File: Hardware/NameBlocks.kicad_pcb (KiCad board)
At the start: 2 copper layers, 38.1 x 38.1 mm, 19 parts, among them J1 CONN_01X06, J2 CONN_01X05, J3 CONN_01X05, Q1 Q_NMOS_GSD, U1 ACPSA04-41SRWA-17406, U2 ATTiny828, U3 MAX16054

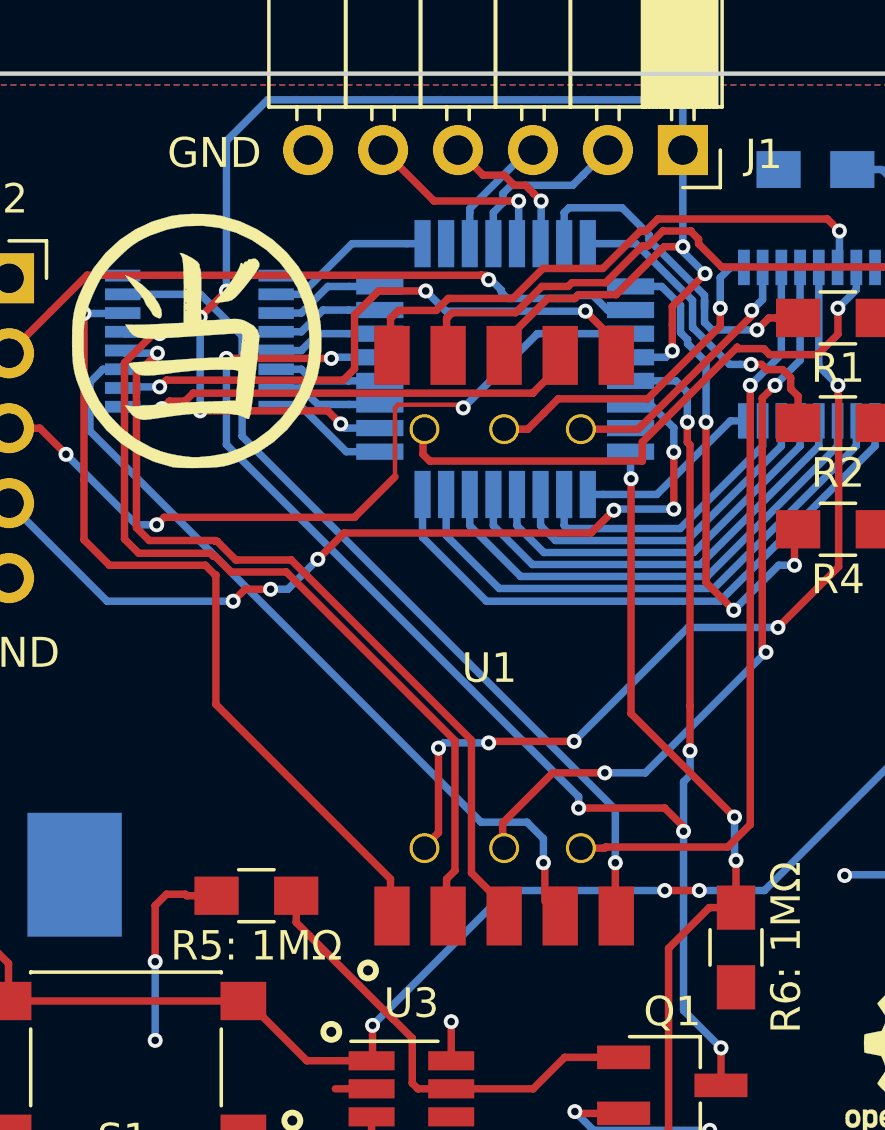
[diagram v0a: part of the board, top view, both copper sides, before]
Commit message: Shrank trace on Net-(RN2-Pad1) for pin 13 of display
Pins 13, 14, 15, 16 on the LED segment shorted together on two boards AFTER soldering the display down. I believe that is because trace Net-(RN2-Pad1) from pin 13 on the alphanumeric display was too close to pins 14, 15, 16, resulting in a short after soldering and when the display is pressed down. I changed that trace to 6 mils (from 10 mils) and moved it away from the problem zone.
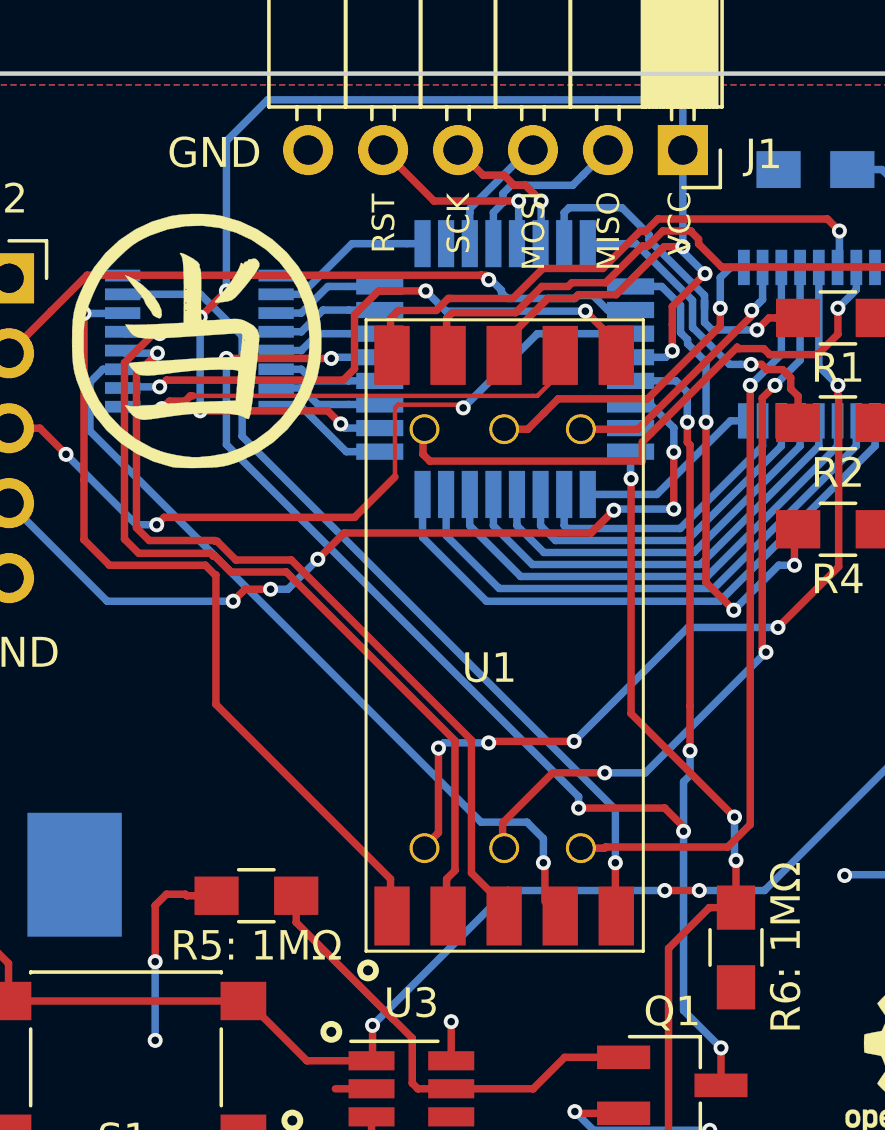
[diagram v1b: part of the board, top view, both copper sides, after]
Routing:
- net Net-(RN2-Pad1): track 15.8 -> 16.4 mm
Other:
- board text added: "1.1"
- board text added: "MISO"
- board text added: "MOSI"
- board text added: "March 2018, v1.1"
- board text added: "RST"
- board text added: "SCK"
- board text removed: "1.0"
- board text removed: "Feb 2018, v1.0"
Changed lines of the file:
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@@
     (area 68.821399 34.175799 271.609914 194.5424)
     (thickness 1.6)
-    (drawings 26)
-    (tracks 540)
+    (drawings 31)
+    (tracks 542)
     (zones 0)
     (modules 19)
@@
   (page A4)
   (layers
-    (0 F.Cu signal hide)
-    (31 B.Cu signal hide)
+    (0 F.Cu signal)
+    (31 B.Cu signal)
     (32 B.Adhes user)
     (33 F.Adhes user)
@@
     (47 F.CrtYd user)
     (48 B.Fab user hide)
-    (49 F.Fab user hide)
+    (49 F.Fab user)
   )
   (setup
@@
     (add_net "Net-(RN2-Pad7)")
     (add_net VCC)
+  )
+  (module ACPSA04_Alphanumeric_LED:ACPSA04_Alphanumeric_LED locked (layer F.Cu)
+    (at 91.7788 51.6124)
+    (fp_text reference U1 (at 3.8 10.6) (layer F.SilkS)
+      (effects (font (size 1 1) (thickness 0.15)))
+    )
+    (fp_text value ACPSA04-41SRWA-17406 (at 5.3 8.8) (layer F.Fab)
+      (effects (font (size 1 1) (thickness 0.15)))
+    )
+    (fp_line (start -0.381 20.193) (end -0.381 -1.2065) (layer F.SilkS) (width 0.1016))
+    (fp_line (start 9.017 20.193) (end -0.381 20.193) (layer F.SilkS) (width 0.1016))
+    (fp_line (start 9.017 -1.2065) (end 9.017 20.193) (layer F.SilkS) (width 0.1016))
+    (fp_line (start -0.381 -1.2065) (end 9.017 -1.2065) (layer F.SilkS) (width 0.1016))
+    (fp_line (start -0.4 20.2) (end -0.4 -1.2) (layer F.CrtYd) (width 0.1016))
+    (fp_line (start 9 20.2) (end -0.4 20.2) (layer F.CrtYd) (width 0.1016))
+    (fp_line (start 9 -1.2) (end 9 20.2) (layer F.CrtYd) (width 0.1016))
+    (fp_line (start -0.4 -1.2) (end 9 -1.2) (layer F.CrtYd) (width 0.1016))
+    (pad 16 smd rect (at 0.5 0) (size 1.2 2) (layers F.Cu F.Paste F.Mask)
+      (net 19 "Net-(RN1-Pad6)"))
+    (pad 15 smd rect (at 2.4 0) (size 1.2 2) (layers F.Cu F.Paste F.Mask)
+      (net 21 "Net-(RN1-Pad8)"))
+    (pad 14 smd rect (at 4.3 0) (size 1.2 2) (layers F.Cu F.Paste F.Mask)
+      (net 1 VCC))
+    (pad 13 smd rect (at 6.2 0) (size 1.2 2) (layers F.Cu F.Paste F.Mask)
+      (net 30 "Net-(RN2-Pad1)"))
+    (pad 12 smd rect (at 8.1 0) (size 1.2 2) (layers F.Cu F.Paste F.Mask)
+      (net 31 "Net-(RN2-Pad2)"))
+    (pad 9 thru_hole circle (at 1.6 2.5) (size 1.016 1.016) (drill 0.8) (layers *.Cu *.Mask)
+      (net 20 "Net-(RN1-Pad7)"))
+    (pad 1 smd rect (at 0.5 19) (size 1.2 2) (layers F.Cu F.Paste F.Mask)
+      (net 35 "Net-(RN2-Pad6)"))
+    (pad 2 smd rect (at 2.4 19) (size 1.2 2) (layers F.Cu F.Paste F.Mask)
+      (net 34 "Net-(RN2-Pad5)"))
+    (pad 3 smd rect (at 4.3 19) (size 1.2 2) (layers F.Cu F.Paste F.Mask)
+      (net 33 "Net-(RN2-Pad4)"))
+    (pad 4 smd rect (at 6.2 19) (size 1.2 2) (layers F.Cu F.Paste F.Mask)
+      (net 32 "Net-(RN2-Pad3)"))
+    (pad 5 smd rect (at 8.1 19) (size 1.2 2) (layers F.Cu F.Paste F.Mask)
+      (net 36 "Net-(RN2-Pad7)"))
+    (pad 10 thru_hole circle (at 4.3 2.5) (size 1.016 1.016) (drill 0.8) (layers *.Cu *.Mask)
+      (net 14 "Net-(RN1-Pad1)"))
+    (pad 11 thru_hole circle (at 6.9 2.5) (size 1.016 1.016) (drill 0.8) (layers *.Cu *.Mask)
+      (net 15 "Net-(RN1-Pad2)"))
+    (pad 7 thru_hole circle (at 4.3 16.7) (size 1.016 1.016) (drill 0.8) (layers *.Cu *.Mask)
+      (net 17 "Net-(RN1-Pad4)"))
+    (pad 8 thru_hole circle (at 1.6 16.7) (size 1.016 1.016) (drill 0.8) (layers *.Cu *.Mask)
+      (net 18 "Net-(RN1-Pad5)"))
+    (pad 6 thru_hole circle (at 6.9 16.7) (size 1.016 1.016) (drill 0.8) (layers *.Cu *.Mask)
+      (net 16 "Net-(RN1-Pad3)"))
   )
   (module Buttons_Switches_SMD:SW_SPST_PTS645 locked (layer F.Cu)
@@
       (xy 0.376964 -2.709982)) (layer F.SilkS) (width 0.01))
   )
-  (module ACPSA04_Alphanumeric_LED:ACPSA04_Alphanumeric_LED locked (layer F.Cu)
-    (at 91.7788 51.6124)
-    (fp_text reference U1 (at 3.8 10.6) (layer F.SilkS)
-      (effects (font (size 1 1) (thickness 0.15)))
-    )
-    (fp_text value ACPSA04-41SRWA-17406 (at 5.3 8.8) (layer F.Fab)
-      (effects (font (size 1 1) (thickness 0.15)))
-    )
-    (fp_line (start -0.4 20.2) (end -0.4 -1.2) (layer F.CrtYd) (width 0.1016))
-    (fp_line (start 9 20.2) (end -0.4 20.2) (layer F.CrtYd) (width 0.1016))
-    (fp_line (start 9 -1.2) (end 9 20.2) (layer F.CrtYd) (width 0.1016))
-    (fp_line (start -0.4 -1.2) (end 9 -1.2) (layer F.CrtYd) (width 0.1016))
-    (pad 16 smd rect (at 0.5 0) (size 1.2 2) (layers F.Cu F.Paste F.Mask)
-      (net 19 "Net-(RN1-Pad6)"))
-    (pad 15 smd rect (at 2.4 0) (size 1.2 2) (layers F.Cu F.Paste F.Mask)
-      (net 21 "Net-(RN1-Pad8)"))
-    (pad 14 smd rect (at 4.3 0) (size 1.2 2) (layers F.Cu F.Paste F.Mask)
-      (net 1 VCC))
-    (pad 13 smd rect (at 6.2 0) (size 1.2 2) (layers F.Cu F.Paste F.Mask)
-      (net 30 "Net-(RN2-Pad1)"))
-    (pad 12 smd rect (at 8.1 0) (size 1.2 2) (layers F.Cu F.Paste F.Mask)
-      (net 31 "Net-(RN2-Pad2)"))
-    (pad 9 thru_hole circle (at 1.6 2.5) (size 1.016 1.016) (drill 0.8) (layers *.Cu *.Mask)
-      (net 20 "Net-(RN1-Pad7)"))
-    (pad 1 smd rect (at 0.5 19) (size 1.2 2) (layers F.Cu F.Paste F.Mask)
-      (net 35 "Net-(RN2-Pad6)"))
-    (pad 2 smd rect (at 2.4 19) (size 1.2 2) (layers F.Cu F.Paste F.Mask)
-      (net 34 "Net-(RN2-Pad5)"))
-    (pad 3 smd rect (at 4.3 19) (size 1.2 2) (layers F.Cu F.Paste F.Mask)
-      (net 33 "Net-(RN2-Pad4)"))
-    (pad 4 smd rect (at 6.2 19) (size 1.2 2) (layers F.Cu F.Paste F.Mask)
-      (net 32 "Net-(RN2-Pad3)"))
-    (pad 5 smd rect (at 8.1 19) (size 1.2 2) (layers F.Cu F.Paste F.Mask)
-      (net 36 "Net-(RN2-Pad7)"))
-    (pad 10 thru_hole circle (at 4.3 2.5) (size 1.016 1.016) (drill 0.8) (layers *.Cu *.Mask)
-      (net 14 "Net-(RN1-Pad1)"))
-    (pad 11 thru_hole circle (at 6.9 2.5) (size 1.016 1.016) (drill 0.8) (layers *.Cu *.Mask)
-      (net 15 "Net-(RN1-Pad2)"))
-    (pad 7 thru_hole circle (at 4.3 16.7) (size 1.016 1.016) (drill 0.8) (layers *.Cu *.Mask)
-      (net 17 "Net-(RN1-Pad4)"))
-    (pad 8 thru_hole circle (at 1.6 16.7) (size 1.016 1.016) (drill 0.8) (layers *.Cu *.Mask)
-      (net 18 "Net-(RN1-Pad5)"))
-    (pad 6 thru_hole circle (at 6.9 16.7) (size 1.016 1.016) (drill 0.8) (layers *.Cu *.Mask)
-      (net 16 "Net-(RN1-Pad3)"))
+  (gr_text VCC (at 102.0318 47.1424 90) (layer F.SilkS)
+    (effects (font (size 0.762 0.762) (thickness 0.1524)))
+  )
+  (gr_text MISO (at 99.6188 47.3964 90) (layer F.SilkS)
+    (effects (font (size 0.762 0.762) (thickness 0.1524)))
+  )
+  (gr_text MOSI (at 97.0788 47.3964 90) (layer F.SilkS)
+    (effects (font (size 0.762 0.762) (thickness 0.1524)))
+  )
+  (gr_text SCK (at 94.5388 47.1424 90) (layer F.SilkS)
+    (effects (font (size 0.762 0.762) (thickness 0.1524)))
+  )
+  (gr_text RST (at 91.9988 47.1424 90) (layer F.SilkS)
+    (effects (font (size 0.762 0.762) (thickness 0.1524)))
   )
   (dimension 38.1 (width 0.3) (layer Dwgs.User)
@@
     (arrow2b (pts (xy 77.0128 82.4484) (xy 78.139304 81.861979)))
   )
-  (gr_text "Feb 2018, v1.0" (at 110.109 43.4086) (layer B.SilkS)
+  (gr_text "March 2018, v1.1" (at 109.2708 43.3324) (layer B.SilkS)
     (effects (font (size 0.762 0.762) (thickness 0.1524)) (justify mirror))
   )
-  (gr_text github.com/Erik-k/NameBlocks (at 95.7326 58.293) (layer B.SilkS)
+  (gr_text github.com/Erik-k/NameBlocks (at 96.0628 57.9374) (layer B.SilkS)
     (effects (font (size 0.762 0.762) (thickness 0.1)) (justify mirror))
   )
@@
   (gr_line (start 115.1128 42.0624) (end 115.1128 80.1624) (layer Edge.Cuts) (width 0.15))
   (gr_line (start 77.0128 42.0624) (end 115.1128 42.0624) (layer Edge.Cuts) (width 0.15))
-  (gr_text 1.0 (at 269.8242 193.0908) (layer F.Fab)
+  (gr_text 1.1 (at 269.8242 193.0908) (layer F.Fab)
     (effects (font (size 1.5 1.5) (thickness 0.3)))
   )
@@
   (segment (start 101.2553 56.326) (end 99.4422 56.326) (width 0.254) (layer B.Cu) (net 29))
   (segment (start 99.4422 56.326) (end 98.9132 56.326) (width 0.254) (layer B.Cu) (net 29))
-  (segment (start 97.048599 52.891801) (end 85.538199 52.891801) (width 0.254) (layer F.Cu) (net 30))
-  (segment (start 85.538199 52.891801) (end 85.267799 53.162201) (width 0.254) (layer F.Cu) (net 30))
+  (segment (start 97.2058 52.9844) (end 97.9788 52.2114) (width 0.1524) (layer F.Cu) (net 30))
+  (segment (start 97.9788 52.2114) (end 97.9788 51.6124) (width 0.254) (layer F.Cu) (net 30))
+  (segment (start 97.048599 52.9844) (end 97.2058 52.9844) (width 0.1524) (layer F.Cu) (net 30))
+  (segment (start 85.538199 52.9844) (end 85.4456 52.9844) (width 0.254) (layer F.Cu) (net 30))
+  (segment (start 85.4456 52.9844) (end 85.267799 53.162201) (width 0.254) (layer F.Cu) (net 30))
+  (segment (start 97.048599 52.9844) (end 85.538199 52.9844) (width 0.1524) (layer F.Cu) (net 30))
   (segment (start 85.267799 53.162201) (end 84.734399 53.162201) (width 0.254) (layer F.Cu) (net 30))
   (segment (start 84.734399 53.162201) (end 84.4804 53.4162) (width 0.254) (layer F.Cu) (net 30))
-  (segment (start 97.048599 52.891801) (end 97.018999 52.891801) (width 0.254) (layer F.Cu) (net 30))
   (segment (start 84.4804 53.4162) (end 83.2139 53.4162) (width 0.254) (layer B.Cu) (net 30))
   (segment (start 83.2139 53.4162) (end 83.1504 53.3527) (width 0.254) (layer B.Cu) (net 30))
   (segment (start 97.928 51.6124) (end 97.928 52.0124) (width 0.254) (layer F.Cu) (net 30))
-  (segment (start 97.928 52.0124) (end 97.048599 52.891801) (width 0.254) (layer F.Cu) (net 30))
   (via (at 84.4804 53.4162) (size 0.508) (drill 0.254) (layers F.Cu B.Cu) (net 30))
   (segment (start 84.4042 52.6796) (end 83.1885 52.6796) (width 0.254) (layer B.Cu) (net 31))

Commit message: Added note to fix TSSOP footprints
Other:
- board text added: "Extend the pads on the two RN1 RN2 TSSOP packages outward Change trace widths down to 6 mils if necessary"
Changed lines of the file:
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@@
     (area 68.821399 34.175799 271.609914 194.5424)
     (thickness 1.6)
-    (drawings 31)
+    (drawings 32)
     (tracks 542)
     (zones 0)
@@
       (xy 0.376964 -2.709982)) (layer F.SilkS) (width 0.01))
   )
+  (gr_text "Extend the pads on the two RN1 RN2 TSSOP packages outward\nChange trace widths down to 6 mils if necessary" (at 109.2708 25.1714) (layer F.Fab)
+    (effects (font (size 2.032 2.032) (thickness 0.3)))
+  )
   (gr_text VCC (at 102.0318 47.1424 90) (layer F.SilkS)
